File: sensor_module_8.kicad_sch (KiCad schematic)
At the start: 47 parts, among them J10 Conn_Coaxial, J11 Conn_Coaxial, J16 SLOT 1, J17 Conn_Coaxial, J18 Conn_Coaxial, J19 Conn_Coaxial, J20 Conn_Coaxial, J8 Conn_Coaxial, J9 Conn_Coaxial, U14 INA333xxDGK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

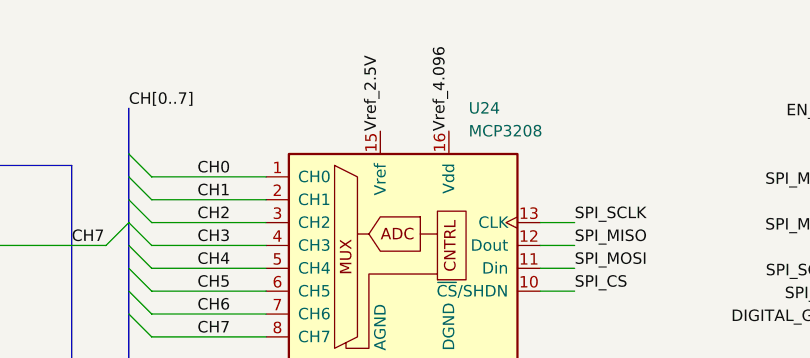
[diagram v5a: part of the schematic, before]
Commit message: Updated the ORP and pH probes with a more appropriate amp. Added some notes. Added a tentative PL-100 adapter circuit. Added Vref buffering. Started move towards ESP32 ADC converter for base sensors.
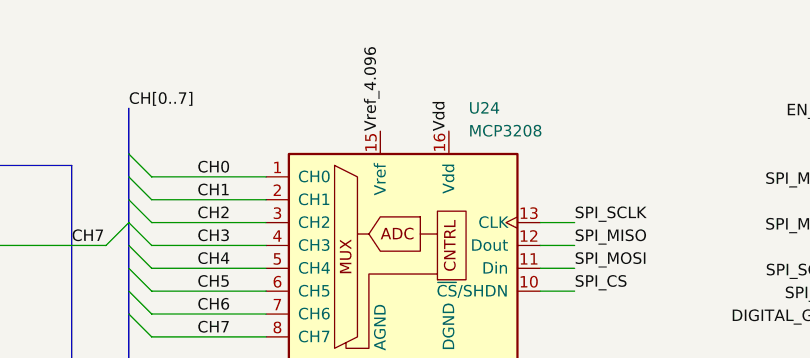
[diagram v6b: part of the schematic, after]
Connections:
- net Vref_2.5V is gone; now on net Vref_4.096: U24.15 (Vref)
- net Vdd: now also U24.16 (Vdd)
- net Vref_4.096: no longer U24.16 (Vdd)
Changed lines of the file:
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@@
+		)
+	)
+	(label "Vdd"
+		(at 208.28 24.13 90)
+		(effects
+			(font
+				(size 1.27 1.27)
+			)
+			(justify left bottom)
 		)
 	)
@@
 	)
 	(label "Vref_4.096"
-		(at 208.28 24.13 90)
+		(at 200.66 24.13 90)
 		(effects
 			(font
@@
 		(effects
 			(font
-				(size 1.27 1.27)
-			)
-			(justify left bottom)
-		)
-	)
-	(label "Vref_2.5V"
-		(at 200.66 24.13 90)
-		(effects
-			(font
